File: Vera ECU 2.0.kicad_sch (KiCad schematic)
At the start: 30 parts

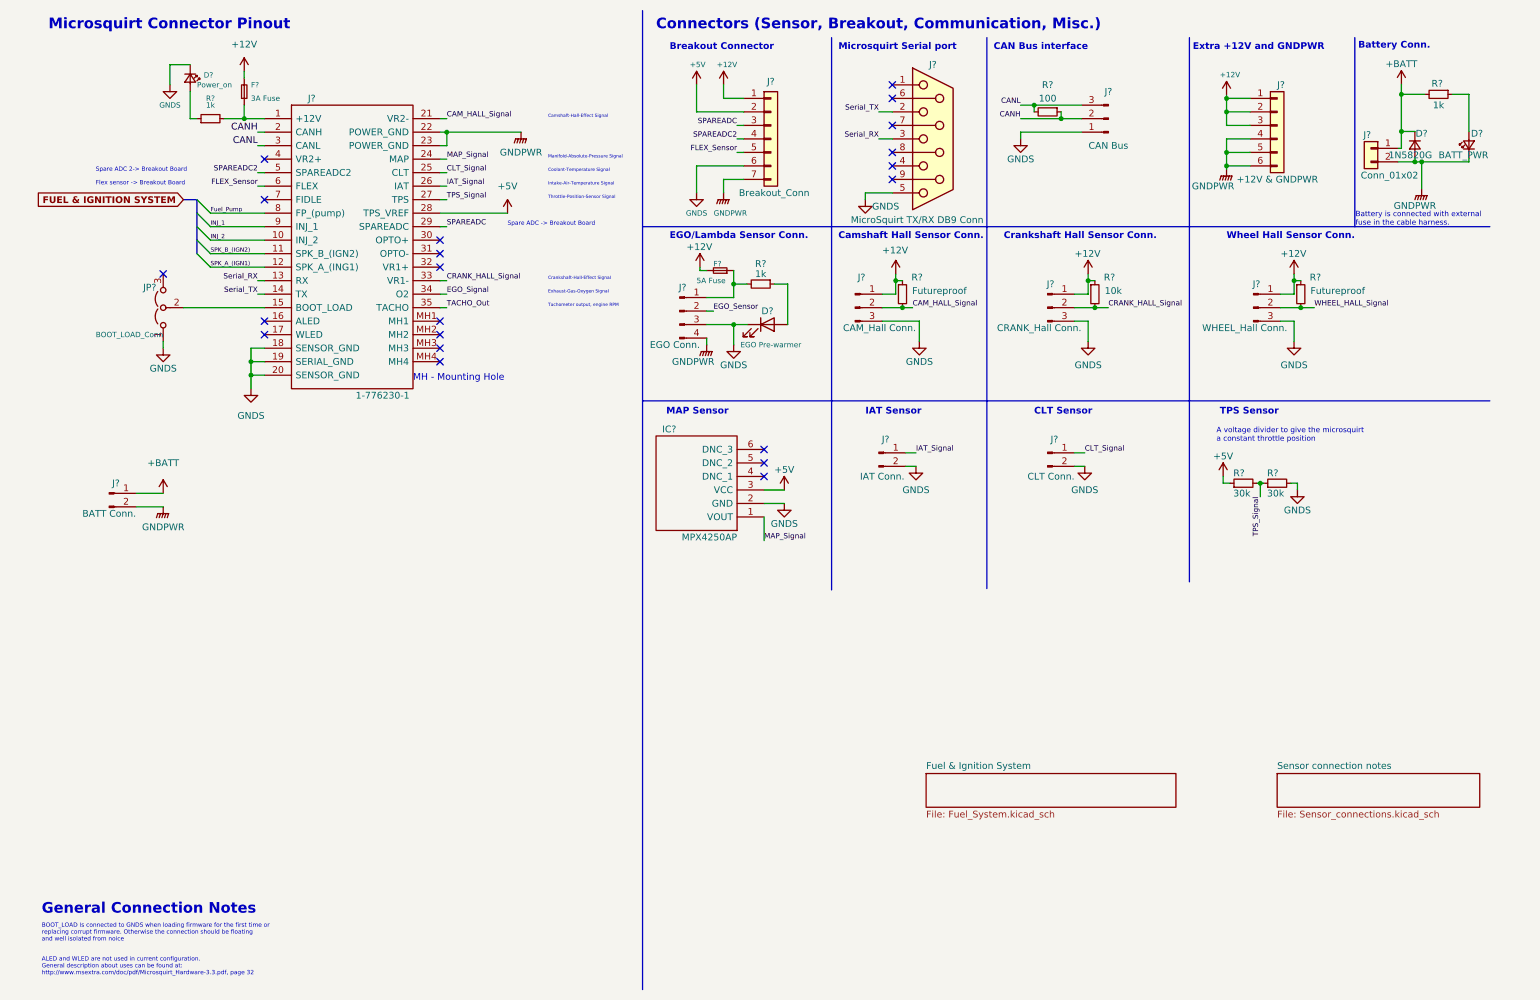
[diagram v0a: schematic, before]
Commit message: Added more connectors to schematic
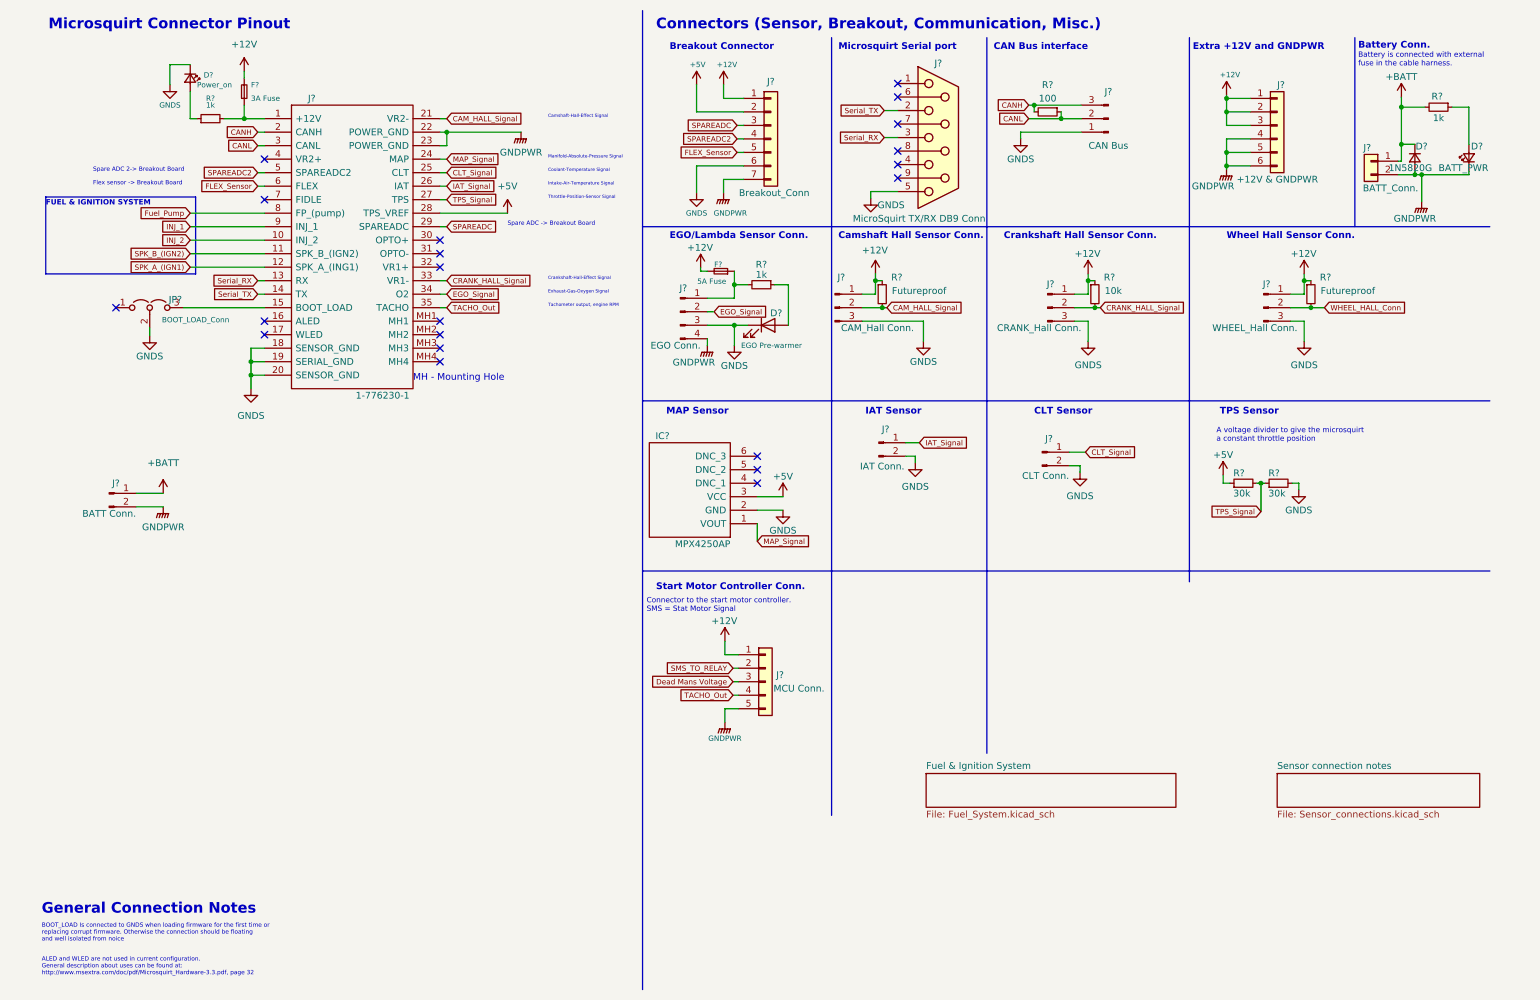
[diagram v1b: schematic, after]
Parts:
- added J?: MCU Conn., symbol Connector_Generic:Conn_01x05
- J?: value Conn_01x02 -> BATT_Conn.
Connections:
- net EGO_Sensor is gone; now on net EGO_Signal: J?.2 (Pin_2)
- net +12V: now also J?.1 (Pin_1)
- net CANH: now also J?.3 (Pin_3), R?.2; no longer J?.2 (Pin_2), R?.1
- net CANL: now also J?.2 (Pin_2), R?.1; no longer J?.3 (Pin_3), R?.2
- net GNDPWR: now also J?.5 (Pin_5)
- net GNDS: now also JP?.2 (C); no longer JP?.1 (A)
- net TACHO_Out: now also J?.4 (Pin_4)
- net at J?.15 (BOOT_LOAD): now also JP?.3 (B); no longer JP?.2 (C)
- net WHEEL_HALL_Signal renamed WHEEL_HALL_Conn
- new net Dead Mans Voltage: J?.3 (Pin_3)
- new net SMS_TO_RELAY: J?.2 (Pin_2)
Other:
- note added: "Connector to the start motor controller. SMS = Stat Motor Signal"
- note added: "FUEL & IGNITION SYSTEM"
- note added: "Start Motor Controller Conn."
- moved on the sheet: D?, IC?, J?, JP?, R?
